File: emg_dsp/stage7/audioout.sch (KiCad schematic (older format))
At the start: 17 parts, among them U94 MIC5365-2.5, U95 AD5663, U96 LM4808, U97 AUDIO_JACK

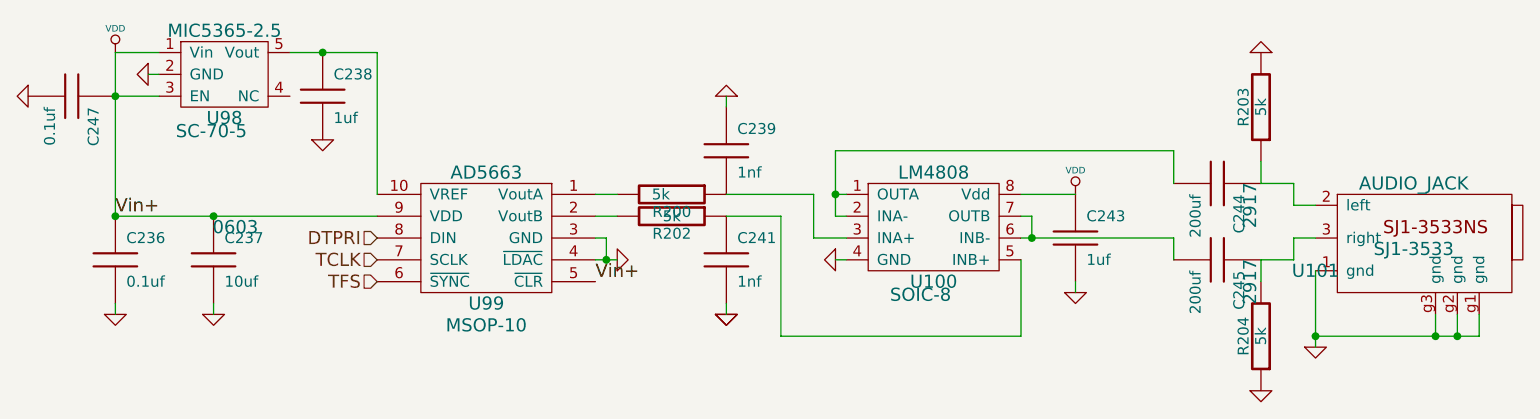
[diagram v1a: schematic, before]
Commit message: adding changes to new board -- still feel that the schematic needs to be checked over, though.
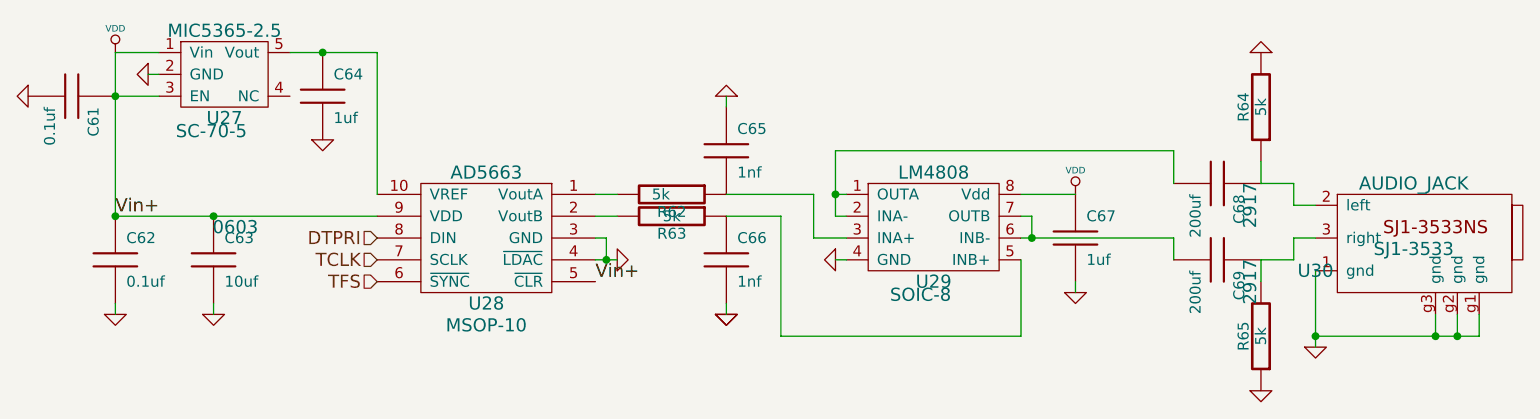
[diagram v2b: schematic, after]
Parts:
- renumbered C246 to C61, C226 to C62, C227 to C63, C228 to C64, C229 to C65, C231 to C66, C233 to C67, C234 to C68, C235 to C69, R195 to R62, R197 to R63, R198 to R64, R199 to R65, U94 to U27, U95 to U28, U96 to U29, U97 to U30

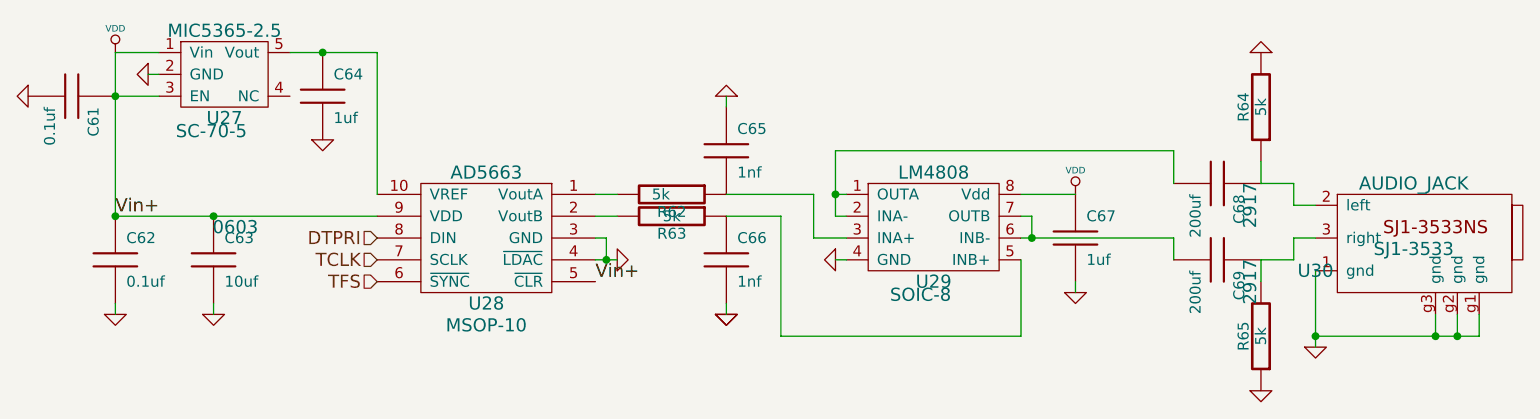
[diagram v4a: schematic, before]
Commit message: starting placement of modules in board...
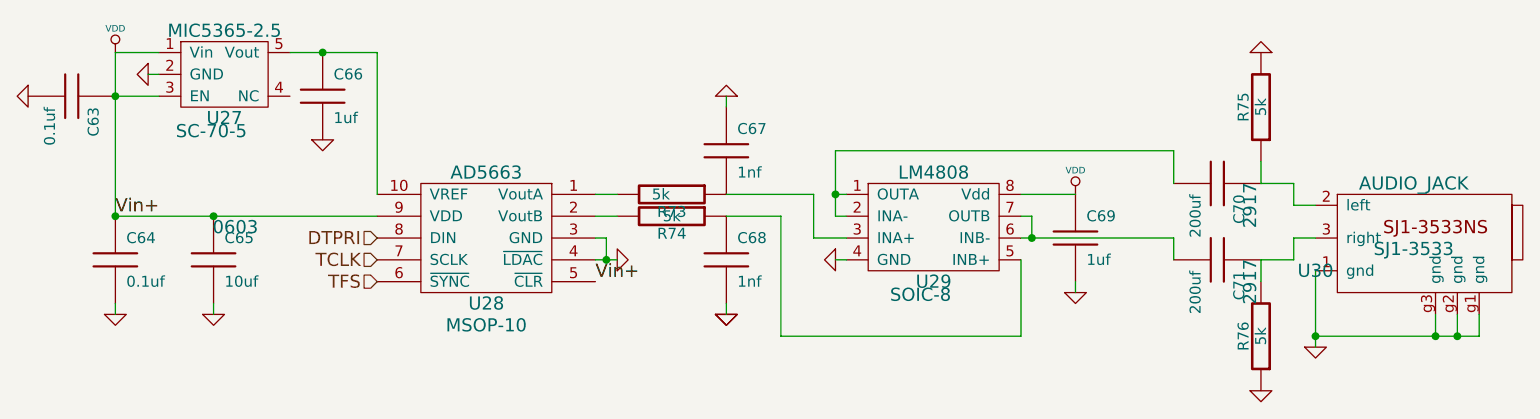
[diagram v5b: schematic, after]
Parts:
- renumbered C61 to C63, C62 to C64, C63 to C65, C64 to C66, C65 to C67, C66 to C68, C67 to C69, C68 to C70, C69 to C71, R62 to R73, R63 to R74, R64 to R75, R65 to R76
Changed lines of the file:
@@
-EESchema Schematic File Version 2  date Fri 21 Jan 2011 05:22:11 PM EST
+EESchema Schematic File Version 2  date Fri 21 Jan 2011 07:08:04 PM EST
 LIBS:power
 LIBS:device
@@
 Sheet 19 19
 Title ""
-Date "21 jan 2011"
+Date "22 jan 2011"
 Rev ""
 Comp ""
@@
 $EndDescr
 $Comp
-L VDD #PWR0222
+L VDD #PWR0169
 U 1 1 4CACDD2B
 P 6100 3000
-F 0 "#PWR0222" H 6100 3100 30  0001 C CNN
+F 0 "#PWR0169" H 6100 3100 30  0001 C CNN
 F 1 "VDD" H 6100 3110 30  0000 C CNN
 	1    6100 3000
@@
 $EndComp
 $Comp
-L VDD #PWR0223
+L VDD #PWR0170
 U 1 1 4CACDD1E
 P 1700 2350
-F 0 "#PWR0223" H 1700 2450 30  0001 C CNN
+F 0 "#PWR0170" H 1700 2450 30  0001 C CNN
 F 1 "VDD" H 1700 2460 30  0000 C CNN
 	1    1700 2350
@@
 	6950 2950 6950 2850
 $Comp
-L GND #PWR0224
+L GND #PWR0171
 U 1 1 4CA4FCDF
 P 1300 2550
-F 0 "#PWR0224" H 1300 2550 30  0001 C CNN
+F 0 "#PWR0171" H 1300 2550 30  0001 C CNN
 F 1 "GND" H 1300 2480 30  0001 C CNN
 	1    1300 2550
@@
 $EndComp
 $Comp
-L C C61
+L C C63
 U 1 1 4CA4FCDA
 P 1500 2550
-F 0 "C61" H 1550 2650 50  0000 L CNN
+F 0 "C63" H 1550 2650 50  0000 L CNN
 F 1 "0.1uf" H 1550 2450 50  0000 L CNN
 F 2 "0402" H 1600 2700 60  0001 C CNN
@@
 $EndComp
 $Comp
-L GND #PWR0225
+L GND #PWR0172
 U 1 1 4CA4E84E
 P 6950 3900
-F 0 "#PWR0225" H 6950 3900 30  0001 C CNN
+F 0 "#PWR0172" H 6950 3900 30  0001 C CNN
 F 1 "GND" H 6950 3830 30  0001 C CNN
 	1    6950 3900
@@
 $EndComp
 $Comp
-L GND #PWR0226
+L GND #PWR0173
 U 1 1 4CA4E84C
 P 6950 2350
-F 0 "#PWR0226" H 6950 2350 30  0001 C CNN
+F 0 "#PWR0173" H 6950 2350 30  0001 C CNN
 F 1 "GND" H 6950 2280 30  0001 C CNN
 	1    6950 2350
@@
 $EndComp
 $Comp
-L R R64
+L R R75
 U 1 1 4CA4E848
 P 6950 2600
-F 0 "R64" V 7030 2600 50  0000 C CNN
+F 0 "R75" V 7030 2600 50  0000 C CNN
 F 1 "5k" V 6950 2600 50  0000 C CNN
 F 2 "0402" V 7080 2550 60  0001 C CNN
@@
 $EndComp
 $Comp
-L R R65
+L R R76
 U 1 1 4CA4E841
 P 6950 3650
-F 0 "R65" V 7030 3650 50  0000 C CNN
+F 0 "R76" V 7030 3650 50  0000 C CNN
 F 1 "5k" V 6950 3650 50  0000 C CNN
 F 2 "0402" V 7080 3600 60  0001 C CNN
@@
 $EndComp
 $Comp
-L GND #PWR0227
+L GND #PWR0174
 U 1 1 4CA4E7B7
 P 2650 2750
-F 0 "#PWR0227" H 2650 2750 30  0001 C CNN
+F 0 "#PWR0174" H 2650 2750 30  0001 C CNN
 F 1 "GND" H 2650 2680 30  0001 C CNN
 	1    2650 2750
@@
 $EndComp
 $Comp
-L C C64
+L C C66
 U 1 1 4CA4E79D
 P 2650 2550
-F 0 "C64" H 2700 2650 50  0000 L CNN
+F 0 "C66" H 2700 2650 50  0000 L CNN
 F 1 "1uf" H 2700 2450 50  0000 L CNN
 F 2 "0402" H 2750 2700 60  0001 C CNN
@@
 $EndComp
 $Comp
-L GND #PWR0228
+L GND #PWR0175
 U 1 1 4CA4E788
 P 1850 2450
-F 0 "#PWR0228" H 1850 2450 30  0001 C CNN
+F 0 "#PWR0175" H 1850 2450 30  0001 C CNN
 F 1 "GND" H 1850 2380 30  0001 C CNN
 	1    1850 2450
@@
 $EndComp
 $Comp
-L C C69
+L C C71
 U 1 1 4CA4E6EE
 P 6750 3300
-F 0 "C69" H 6800 3400 50  0000 L CNN
+F 0 "C71" H 6800 3400 50  0000 L CNN
 F 1 "200uf" H 6800 3200 50  0000 L CNN
 F 2 "2917" H 6850 3450 60  0000 C CNN
@@
 $EndComp
 $Comp
-L GND #PWR0229
+L GND #PWR0176
 U 1 1 4CA4E6A8
 P 7200 3700
-F 0 "#PWR0229" H 7200 3700 30  0001 C CNN
+F 0 "#PWR0176" H 7200 3700 30  0001 C CNN
 F 1 "GND" H 7200 3630 30  0001 C CNN
 	1    7200 3700
@@
 $EndComp
 $Comp
-L C C68
+L C C70
 U 1 1 4CA4E661
 P 6750 2950
-F 0 "C68" H 6800 3050 50  0000 L CNN
+F 0 "C70" H 6800 3050 50  0000 L CNN
 F 1 "200uf" H 6800 2850 50  0000 L CNN
 F 2 "2917" H 6850 3100 60  0000 C CNN
@@
 $EndComp
 $Comp
-L GND #PWR0230
+L GND #PWR0177
 U 1 1 4CA4E652
 P 5000 3300
-F 0 "#PWR0230" H 5000 3300 30  0001 C CNN
+F 0 "#PWR0177" H 5000 3300 30  0001 C CNN
 F 1 "GND" H 5000 3230 30  0001 C CNN
 	1    5000 3300
@@
 Vin+
 $Comp
-L GND #PWR0231
+L GND #PWR0178
 U 1 1 4CA4E5F5
 P 4000 3300
-F 0 "#PWR0231" H 4000 3300 30  0001 C CNN
+F 0 "#PWR0178" H 4000 3300 30  0001 C CNN
 F 1 "GND" H 4000 3230 30  0001 C CNN
 	1    4000 3300
@@
 $EndComp
 $Comp
-L GND #PWR0232
+L GND #PWR0179
 U 1 1 4CA4E5B2
 P 4500 2550
-F 0 "#PWR0232" H 4500 2550 30  0001 C CNN
+F 0 "#PWR0179" H 4500 2550 30  0001 C CNN
 F 1 "GND" H 4500 2480 30  0001 C CNN
 	1    4500 2550
@@
 $EndComp
 $Comp
-L R R62
+L R R73
 U 1 1 4CA4E5B0
 P 4250 3000
-F 0 "R62" V 4330 3000 50  0000 C CNN
+F 0 "R73" V 4330 3000 50  0000 C CNN
 F 1 "5k" V 4250 2950 50  0000 C CNN
 F 2 "0402" V 4380 2950 60  0001 C CNN
@@
 $EndComp
 $Comp
-L C C65
+L C C67
 U 1 1 4CA4E5AF
 P 4500 2800
-F 0 "C65" H 4550 2900 50  0000 L CNN
+F 0 "C67" H 4550 2900 50  0000 L CNN
 F 1 "1nf" H 4550 2700 50  0000 L CNN
 F 2 "0402" H 4600 2950 60  0001 C CNN
@@
 $EndComp
 $Comp
-L R R63
+L R R74
 U 1 1 4CA4E5AB
 P 4250 3100
-F 0 "R63" V 4330 3100 50  0000 C CNN
+F 0 "R74" V 4330 3100 50  0000 C CNN
 F 1 "5k" V 4250 3100 50  0000 C CNN
 F 2 "0402" V 4380 3050 60  0001 C CNN
@@
 $EndComp
 $Comp
-L GND #PWR0233
+L GND #PWR0180
 U 1 1 4CA4E5AA
 P 4500 3550
-F 0 "#PWR0233" H 4500 3550 30  0001 C CNN
+F 0 "#PWR0180" H 4500 3550 30  0001 C CNN
 F 1 "GND" H 4500 3480 30  0001 C CNN
 	1    4500 3550
@@
 $EndComp
 $Comp
-L GND #PWR0234
+L GND #PWR0181
 U 1 1 4CA4E599
 P 4500 3550
-F 0 "#PWR0234" H 4500 3550 30  0001 C CNN
+F 0 "#PWR0181" H 4500 3550 30  0001 C CNN
 F 1 "GND" H 4500 3480 30  0001 C CNN
 	1    4500 3550
@@
 $EndComp
 $Comp
-L C C66
+L C C68
 U 1 1 4CA4E4D2
 P 4500 3300
-F 0 "C66" H 4550 3400 50  0000 L CNN
+F 0 "C68" H 4550 3400 50  0000 L CNN
 F 1 "1nf" H 4550 3200 50  0000 L CNN
 F 2 "0402" H 4600 3450 60  0001 C CNN
@@
 $EndComp
 $Comp
-L GND #PWR0235
+L GND #PWR0182
 U 1 1 4CA4E4BA
 P 6100 3450
-F 0 "#PWR0235" H 6100 3450 30  0001 C CNN
+F 0 "#PWR0182" H 6100 3450 30  0001 C CNN
 F 1 "GND" H 6100 3380 30  0001 C CNN
 	1    6100 3450
@@
 $EndComp
 $Comp
-L C C67
+L C C69
 U 1 1 4CA4E4AF
 P 6100 3200
-F 0 "C67" H 6150 3300 50  0000 L CNN
+F 0 "C69" H 6150 3300 50  0000 L CNN
 F 1 "1uf" H 6150 3100 50  0000 L CNN
 F 2 "0402" H 6200 3350 60  0001 C CNN
@@
 Vin+
 $Comp
-L GND #PWR0236
+L GND #PWR0183
 U 1 1 4CA4E458
 P 2150 3550
-F 0 "#PWR0236" H 2150 3550 30  0001 C CNN
+F 0 "#PWR0183" H 2150 3550 30  0001 C CNN
 F 1 "GND" H 2150 3480 30  0001 C CNN
 	1    2150 3550
@@
 $EndComp
 $Comp
-L GND #PWR0237
+L GND #PWR0184
 U 1 1 4CA4E455
 P 1700 3550
-F 0 "#PWR0237" H 1700 3550 30  0001 C CNN
+F 0 "#PWR0184" H 1700 3550 30  0001 C CNN
 F 1 "GND" H 1700 3480 30  0001 C CNN
 	1    1700 3550
@@
 $EndComp
 $Comp
-L C C62
+L C C64
 U 1 1 4CA4E420
 P 1700 3300
-F 0 "C62" H 1750 3400 50  0000 L CNN
+F 0 "C64" H 1750 3400 50  0000 L CNN
 F 1 "0.1uf" H 1750 3200 50  0000 L CNN
 F 2 "0402" H 1800 3450 60  0001 C CNN
@@
 $EndComp
 $Comp
-L C C63
+L C C65
 U 1 1 4CA4E411
 P 2150 3300
-F 0 "C63" H 2200 3400 50  0000 L CNN
+F 0 "C65" H 2200 3400 50  0000 L CNN
 F 1 "10uf" H 2200 3200 50  0000 L CNN
 F 2 "0603" H 2250 3450 60  0000 C CNN
